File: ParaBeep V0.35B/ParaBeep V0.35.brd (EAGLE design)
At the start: 35.3 x 57.5 mm, 66 parts, among them IC2 MCP73811/2, Q1 500mA/300V, U1 ADXL345, U2 TPS78330DDCRDDC5_TEX-L, U3 TPS78330DDCRDDC5_TEX-L, U4 UBLOX_SAM_M8Q-0-10, U5 MS5803-14BA, U6 ATSAMD51J20A-A, U7 AT25SF128A-SHB-T, U8 RN4871-V/RM118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

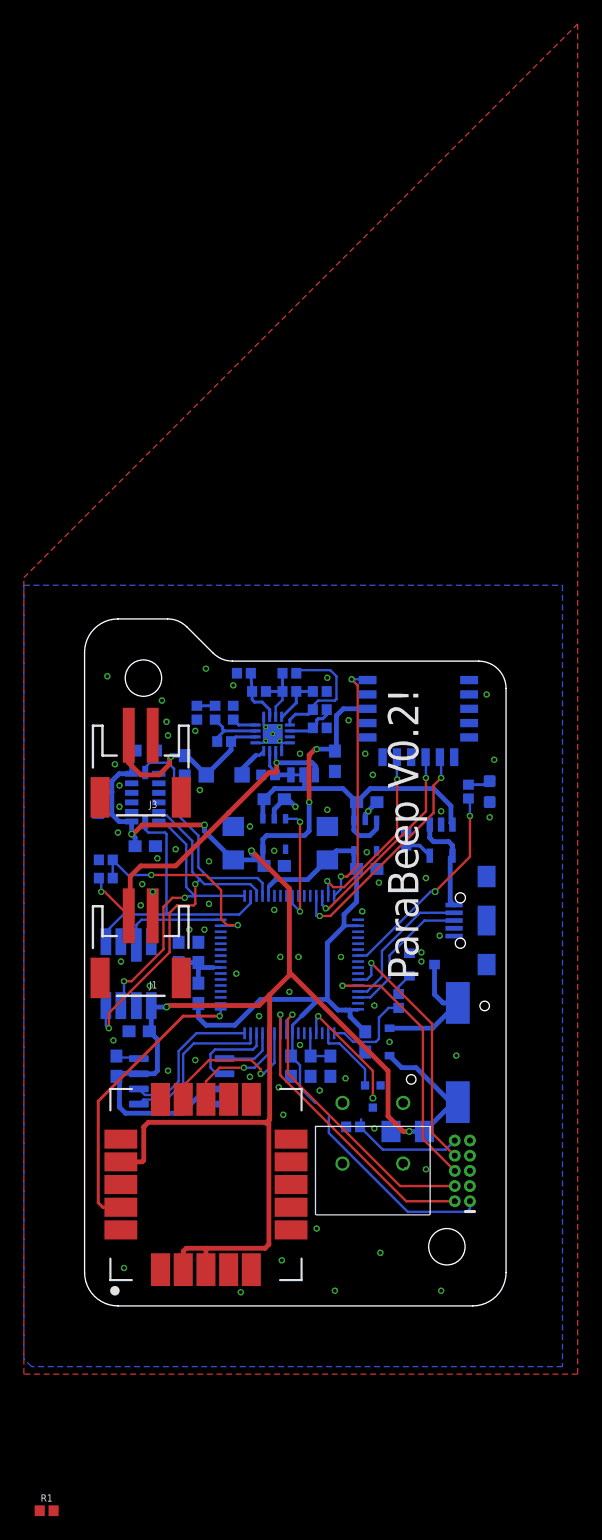
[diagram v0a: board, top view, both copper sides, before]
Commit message: bluetooth working, usb next
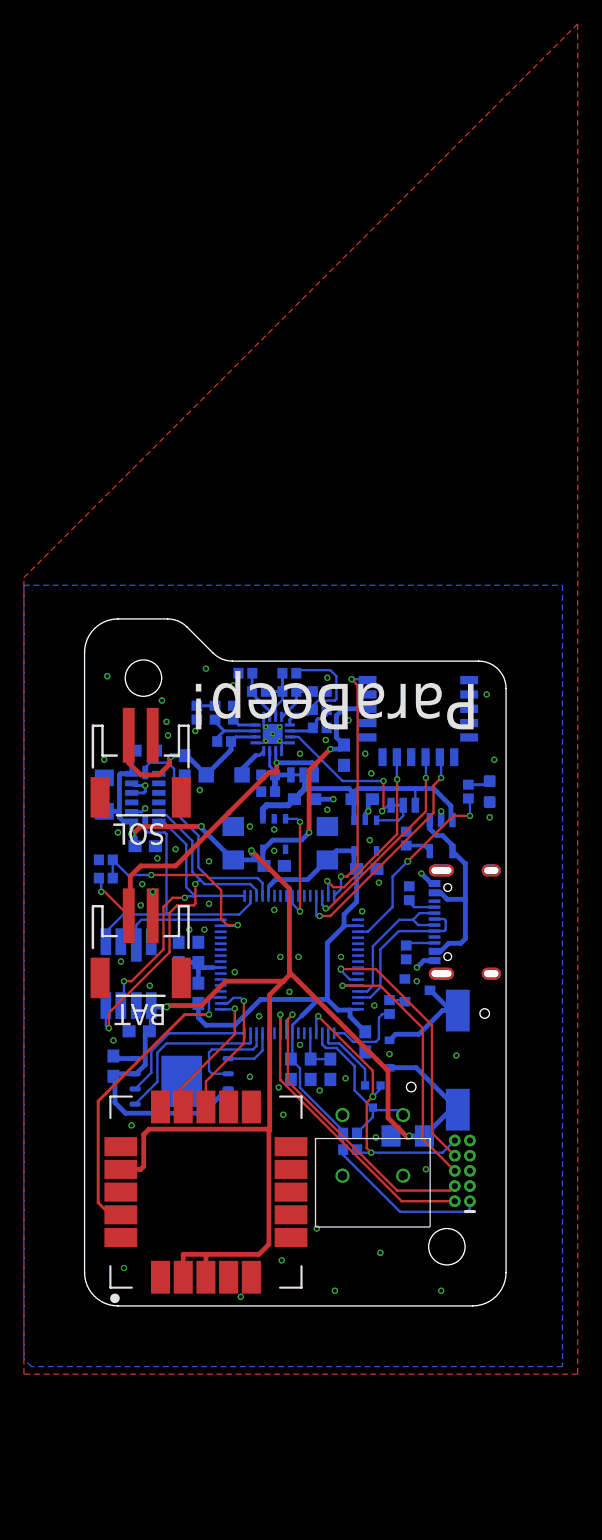
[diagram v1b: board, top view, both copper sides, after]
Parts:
- removed J2: (no value), SparkFun-Connectors:USB-B-MICRO-SMD
- removed U7: AT25SF128A-SHB-T, AT25SF128A-SHB-T:SOIC127P790X216-8N
- added C19: 10uF, SparkFun-Capacitors:EIA3216
- added J4: (no value), SparkFun-Connectors:USB-C-16P-2LAYER-PADS
- added JP2: JUMPER-SMT_3_1-NC_TRACE_SILK, SparkFun-Jumpers:SMT-JUMPER_3_1-NC_TRACE_SILK
- added R2: 5.1K, SparkFun-Resistors:0402
- added R4: 50k, SparkFun-Resistors:0402
- added U10: W25N01GVZEIG_TR, W25N01GVZEIG_TR:SON127P800X600X80-9N
- C17: value 10uF -> 0.01uF; device SparkFun-Capacitors:0603-POLAR -> SparkFun-Capacitors:0402
- C23: value 0.uF -> 4.7uF
- JP3: device SparkFun-Connectors:2X5-PTH-1.27MM@1 -> SparkFun-Connectors:2X5-PTH-1.27MM
- R1: value 10k -> 5.1K
- R25: value (none) -> 4K
- R5: value 10k -> 50k
- moved R1 55.6 mm to (26.9, 29.6), flipped to the bottom, turned to 90 degrees
- moved C17 14.3 mm to (15.4, 43.1), turned to 180 degrees
- moved C5 2.54 mm to (18.4, 42.4)
- moved Q1 2.19 mm to (27.8, 26.4)
- moved U$3 1.02 mm to (24.1, 6.60)
- moved D1 1.02 mm to (25.5, 21.1)
- moved R13 0.92 mm to (25.5, 25.0)
- moved C8 0.92 mm to (21.7, 46.1)
- moved U4 0.63 mm to (10.2, 9.53)
- moved SG1 0.63 mm to (31.2, 20.6)
- moved R5 0.57 mm to (22.2, 14.5), turned to 0 degrees
- moved C2 0.46 mm to (23.2, 42.4)
- moved C1 0.38 mm to (27.1, 14.2)
- moved IC2 0.38 mm to (29.8, 39.4)
- moved C18 0.25 mm to (2.41, 20.1)
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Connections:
- net RX renamed SERCOM3_RX
- net TX renamed SERCOM3_TX
- removed net SERCOM7_RX: U4.13, U6.60
- removed net SERCOM7_TX: U4.14, U6.59
- new net BAT_OK: JP2.3, U9.11
- new net N$4: J4.B5, R1.2
- new net N$5: J4.A5, R2.2
- new net N$6: JP2.2, U2.3
- new net SERCOM1_RX: U4.13, U6.2
- new net SERCOM1_TX: U4.14, U6.1
- net !RESET: now also R4.1; no longer R5.1
- net BUTTON: now also R5.1, U6.51; no longer R1.1
- net CS_MEM: now also U10.1; no longer U7.1
- net D+: now also J4.A6, J4.B6; no longer J2.D+
- net D-: now also J4.A7, J4.B7; no longer J2.D-
- net GND: now also C17.1, C19.-, J4.GND, J4.GND2, JP3.9, R1.1, R2.1, U10.4; no longer C17.-, J2.GND, U7.4
- net GPS_INT: now also U6.3; no longer U6.1
- net LED: now also U6.35; no longer U6.39
- net N$14: now also U10.8; no longer U7.8
- net N$3: now also C17.2
- net SERCOM5_MISO: now also U10.2; no longer U7.2
- net SERCOM5_MOSI: now also U10.5; no longer U7.5
- net SERCOM5_SCK: now also U10.6; no longer U7.6
- net VBUS: now also J4.VBUS1, J4.VBUS2; no longer J2.VBUS
- net VCC-ISO: now also R4.2; no longer R1.2
- net VCC_1: now also C19.+, U10.3, U10.7; no longer C17.+, U7.3, U7.7
- net VIN: now also JP2.1; no longer U2.3
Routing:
- net BUTTON: track 0.00 -> 14.1 mm
- net SERCOM7_TX: track 13.4 -> 0.00 mm, vias 1 -> 0
- net BAT_OK: track 0.00 -> 12.9 mm, vias 0 -> 2
- net SERCOM1_RX: track 0.00 -> 12.4 mm, vias 0 -> 1
- net SERCOM1_TX: track 0.00 -> 11.4 mm, vias 0 -> 1
- net SERCOM7_RX: track 9.42 -> 0.00 mm, vias 1 -> 0
- net VBUS: track 8.47 -> 17.3 mm
- net GND: track 11.6 -> 17.4 mm
- net !RESET: track 19.9 -> 25.2 mm, vias 2 -> 3
- net N$6: track 0.00 -> 3.62 mm
- net VIN: track 27.6 -> 24.9 mm
- net N$5: track 0.00 -> 2.47 mm
- net N$4: track 0.00 -> 2.46 mm
- net D+: track 11.8 -> 14.0 mm
- net SERCOM3_TX: track 21.3 -> 23.1 mm
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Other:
- board text added: "BAT"
- board text added: "ParaBeep!"
- board text added: "SOL"
- board text added: "V0.35B"
- board text removed: "ParaBeep V0.2!"
